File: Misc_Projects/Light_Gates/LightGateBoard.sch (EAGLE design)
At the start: 17 parts, among them T1 PHOTOTRANSISTOR

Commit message: Added changes to LightGateBoard
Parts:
- removed R3: 4.7k, 1-Passive Components:RES_AXIAL1/4W-0.3
- removed T1: PHOTOTRANSISTOR, 1-Active Components:PHOTOTRANSISTOR
- added JP5, JP6: (no value), GTOR - Connectors:PINHD-1X1
- added PH1: PHOTORESISTOR0N1, GTOR - Passive Components:PHOTORESISTOR0N1
- added R6: (no value), GTOR - Passive Components:POTENTIOMETER
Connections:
- net 3V3: now also PH1.1; no longer R3.2
- net GND: now also R6.A; no longer T1.E
- net SIG: now also JP5.1, JP6.1, PH1.2, R6.S; no longer R3.1, T1.C
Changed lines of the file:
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@@
 <layers>
 <layer number="1" name="Top" color="4" fill="1" visible="no" active="no"/>
+<layer number="2" name="Route2" color="16" fill="1" visible="no" active="no"/>
+<layer number="3" name="Route3" color="17" fill="1" visible="no" active="no"/>
+<layer number="4" name="Route4" color="18" fill="1" visible="no" active="no"/>
+<layer number="5" name="Route5" color="19" fill="1" visible="no" active="no"/>
+<layer number="6" name="Route6" color="25" fill="1" visible="no" active="no"/>
+<layer number="7" name="Route7" color="26" fill="1" visible="no" active="no"/>
+<layer number="8" name="Route8" color="27" fill="1" visible="no" active="no"/>
+<layer number="9" name="Route9" color="28" fill="1" visible="no" active="no"/>
+<layer number="10" name="Route10" color="29" fill="1" visible="no" active="no"/>
+<layer number="11" name="Route11" color="30" fill="1" visible="no" active="no"/>
+<layer number="12" name="Route12" color="20" fill="1" visible="no" active="no"/>
+<layer number="13" name="Route13" color="21" fill="1" visible="no" active="no"/>
+<layer number="14" name="Route14" color="22" fill="1" visible="no" active="no"/>
+<layer number="15" name="Route15" color="23" fill="1" visible="no" active="no"/>
 <layer number="16" name="Bottom" color="1" fill="1" visible="no" active="no"/>
 <layer number="17" name="Pads" color="2" fill="1" visible="no" active="no"/>
@@
 <part name="IC1" library="1-Active Components" deviceset="REG_5V_L7805" device="_HOR"/>
 <part name="U$3" library="1-Breakout Boards" deviceset="OLED_SSD1306" device=""/>
-<part name="T1" library="1-Active Components" deviceset="PHOTOTRANSISTOR" device=""/>
 <part name="LED1" library="1-Passive Components" deviceset="LED" device="-5MM" value="Green"/>
-<part name="R3" library="1-Passive Components" deviceset="RES_AXIAL" device="1/4W-0.3" package3d_urn="urn:adsk.eagle:package:23493/2" value="4.7k"/>
 <part name="V1" library="1-Active Components" deviceset="LOGIC_HEX_INVERTER_7404" device="N" package3d_urn="urn:adsk.eagle:package:16407/2"/>
 <part name="R4" library="1-Passive Components" deviceset="RES_AXIAL" device="1/4W-0.3" package3d_urn="urn:adsk.eagle:package:23493/2" value="220"/>
@@
 <part name="LED2" library="1-Passive Components" deviceset="LED" device="-5MM" value="Red"/>
 <part name="JP4" library="1-Connectors" deviceset="PINHD-1X3" device="" package3d_urn="urn:adsk.eagle:package:22458/2"/>
+<part name="PH1" library="GTOR - Passive Components" deviceset="PHOTORESISTOR" device="" package3d_urn="urn:adsk.eagle:package:22223/1" technology="0N1"/>
+<part name="R6" library="GTOR - Passive Components" deviceset="POTENTIOMETER" device="" package3d_urn="urn:adsk.eagle:package:22726/1"/>
+<part name="JP5" library="GTOR - Connectors" deviceset="PINHD-1X1" device="" package3d_urn="urn:adsk.eagle:package:22485/2"/>
+<part name="JP6" library="GTOR - Connectors" deviceset="PINHD-1X1" device="" package3d_urn="urn:adsk.eagle:package:22485/2"/>
 </parts>
 <sheets>
@@
 </instance>
 <instance part="U$3" gate="G$1" x="78.74" y="15.24" smashed="yes"/>
-<instance part="T1" gate="1" x="-104.14" y="58.42" smashed="yes">
-<attribute name="NAME" x="-99.06" y="60.96" size="1.778" layer="95"/>
-<attribute name="VALUE" x="-99.06" y="53.34" size="1.778" layer="96"/>
-</instance>
 <instance part="LED1" gate="LED" x="-38.1" y="88.9" smashed="yes" rot="R90">
 <attribute name="NAME" x="-33.528" y="92.456" size="1.778" layer="95" rot="R180"/>
 <attribute name="VALUE" x="-33.528" y="94.615" size="1.778" layer="96" rot="R180"/>
 </instance>
-<instance part="R3" gate="G$1" x="-101.6" y="76.2" smashed="yes" rot="R90">
-<attribute name="NAME" x="-103.0986" y="72.39" size="1.778" layer="95" rot="R90"/>
-<attribute name="VALUE" x="-98.298" y="72.39" size="1.778" layer="96" rot="R90"/>
-</instance>
 <instance part="V1" gate="/1" x="-73.66" y="88.9" smashed="yes">
 <attribute name="NAME" x="-78.74" y="94.615" size="2.032" layer="95"/>
@@
 <attribute name="NAME" x="62.23" y="56.515" size="1.778" layer="95"/>
 <attribute name="VALUE" x="62.23" y="43.18" size="1.778" layer="96"/>
+</instance>
+<instance part="PH1" gate="G$1" x="-93.98" y="38.1" smashed="yes">
+<attribute name="NAME" x="-91.44" y="38.1" size="1.778" layer="95"/>
+<attribute name="VALUE" x="-91.44" y="35.56" size="1.778" layer="96"/>
+</instance>
+<instance part="R6" gate="G$1" x="-99.06" y="25.4" smashed="yes">
+<attribute name="NAME" x="-102.489" y="21.59" size="1.778" layer="95" rot="R90"/>
+<attribute name="VALUE" x="-102.87" y="21.59" size="1.778" layer="96" rot="R90"/>
+</instance>
+<instance part="JP5" gate="G$1" x="-99.06" y="88.9" smashed="yes" rot="R180">
+<attribute name="NAME" x="-92.71" y="85.725" size="1.778" layer="95" rot="R180"/>
+<attribute name="VALUE" x="-92.71" y="93.98" size="1.778" layer="96" rot="R180"/>
+</instance>
+<instance part="JP6" gate="G$1" x="-99.06" y="81.28" smashed="yes" rot="R180">
+<attribute name="NAME" x="-92.71" y="78.105" size="1.778" layer="95" rot="R180"/>
+<attribute name="VALUE" x="-92.71" y="86.36" size="1.778" layer="96" rot="R180"/>
 </instance>
 </instances>
@@
 </segment>
 <segment>
-<pinref part="T1" gate="1" pin="E"/>
-<wire x1="-101.6" y1="53.34" x2="-101.6" y2="45.72" width="0.1524" layer="91"/>
-<label x="-106.68" y="48.26" size="1.778" layer="95"/>
-</segment>
-<segment>
 <pinref part="LED1" gate="LED" pin="C"/>
 <wire x1="-33.02" y1="88.9" x2="-25.4" y2="88.9" width="0.1524" layer="91"/>
@@
 <label x="55.88" y="50.8" size="1.778" layer="95"/>
 </segment>
+<segment>
+<wire x1="-99.06" y1="20.32" x2="-99.06" y2="12.7" width="0.1524" layer="91"/>
+<label x="-99.06" y="10.16" size="1.778" layer="95"/>
+<pinref part="R6" gate="G$1" pin="A"/>
+</segment>
 </net>
 <net name="5V" class="0">
@@
 </segment>
 <segment>
-<pinref part="R3" gate="G$1" pin="1"/>
-<pinref part="T1" gate="1" pin="C"/>
-<wire x1="-101.6" y1="71.12" x2="-101.6" y2="63.5" width="0.1524" layer="91"/>
-<label x="-106.68" y="68.58" size="1.778" layer="95"/>
-</segment>
-<segment>
 <pinref part="V1" gate="/1" pin="A"/>
+<label x="-88.9" y="88.9" size="1.778" layer="95"/>
 <wire x1="-83.82" y1="88.9" x2="-91.44" y2="88.9" width="0.1524" layer="91"/>
-<label x="-91.44" y="88.9" size="1.778" layer="95"/>
+<pinref part="JP5" gate="G$1" pin="1"/>
+<pinref part="JP6" gate="G$1" pin="1"/>
+<wire x1="-91.44" y1="88.9" x2="-96.52" y2="88.9" width="0.1524" layer="91"/>
+<wire x1="-96.52" y1="81.28" x2="-91.44" y2="81.28" width="0.1524" layer="91"/>
+<wire x1="-91.44" y1="81.28" x2="-91.44" y2="88.9" width="0.1524" layer="91"/>
+<junction x="-91.44" y="88.9"/>
 </segment>
 <segment>
@@
 <wire x1="2.54" y1="76.2" x2="-2.54" y2="76.2" width="0.1524" layer="91"/>
 <label x="-2.54" y="76.2" size="1.778" layer="95"/>
+</segment>
+<segment>
+<wire x1="-93.98" y1="33.02" x2="-93.98" y2="25.4" width="0.1524" layer="91"/>
+<label x="-99.06" y="30.48" size="1.778" layer="95"/>
+<pinref part="PH1" gate="G$1" pin="2"/>
+<pinref part="R6" gate="G$1" pin="S"/>
 </segment>
 </net>
@@
 </segment>
 <segment>
-<pinref part="R3" gate="G$1" pin="2"/>
-<wire x1="-101.6" y1="81.28" x2="-101.6" y2="88.9" width="0.1524" layer="91"/>
-<label x="-106.68" y="86.36" size="1.778" layer="95"/>
-</segment>
-<segment>
 <pinref part="R1" gate="G$1" pin="2"/>
 <wire x1="53.34" y1="33.02" x2="58.42" y2="33.02" width="0.1524" layer="91"/>
@@
 <label x="66.04" y="33.02" size="1.778" layer="95"/>
 </segment>
-</net>
+<segment>
+<pinref part="PH1" gate="G$1" pin="1"/>
+<label x="-93.98" y="60.96" size="1.778" layer="95"/>
+<wire x1="-93.98" y1="58.42" x2="-93.98" y2="43.18" width="0.1524" layer="91"/>
+</segment>
+</net>

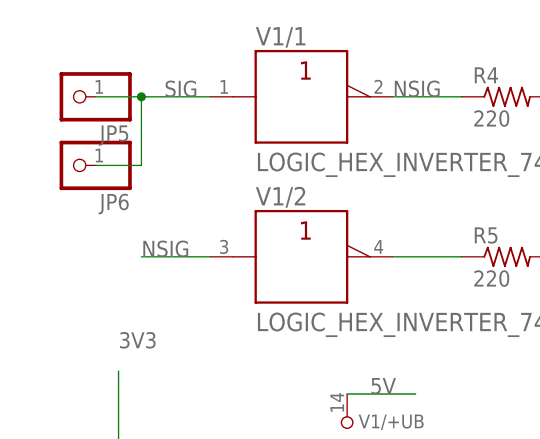
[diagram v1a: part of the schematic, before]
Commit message: Redid PCB with bigger traces and changed photodiode to photoresistor
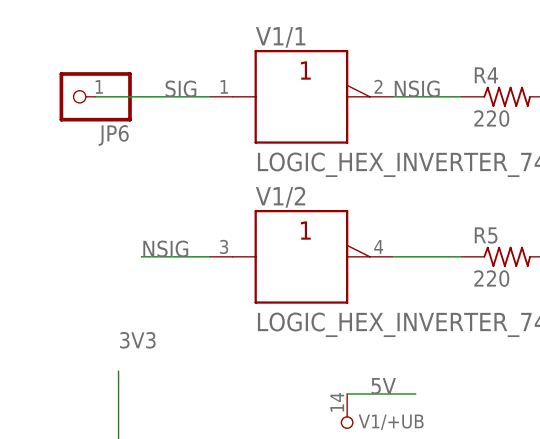
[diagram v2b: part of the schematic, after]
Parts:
- removed JP5: (no value), GTOR - Connectors:PINHD-1X1
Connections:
- net SIG: no longer JP5.1
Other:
- moved on the sheet: JP6
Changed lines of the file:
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@@
 <part name="PH1" library="GTOR - Passive Components" deviceset="PHOTORESISTOR" device="" package3d_urn="urn:adsk.eagle:package:22223/1" technology="0N1"/>
 <part name="R6" library="GTOR - Passive Components" deviceset="POTENTIOMETER" device="" package3d_urn="urn:adsk.eagle:package:22726/1"/>
-<part name="JP5" library="GTOR - Connectors" deviceset="PINHD-1X1" device="" package3d_urn="urn:adsk.eagle:package:22485/2"/>
 <part name="JP6" library="GTOR - Connectors" deviceset="PINHD-1X1" device="" package3d_urn="urn:adsk.eagle:package:22485/2"/>
 </parts>
@@
 <attribute name="VALUE" x="-102.87" y="21.59" size="1.778" layer="96" rot="R90"/>
 </instance>
-<instance part="JP5" gate="G$1" x="-99.06" y="88.9" smashed="yes" rot="R180">
+<instance part="JP6" gate="G$1" x="-99.06" y="88.9" smashed="yes" rot="R180">
 <attribute name="NAME" x="-92.71" y="85.725" size="1.778" layer="95" rot="R180"/>
 <attribute name="VALUE" x="-92.71" y="93.98" size="1.778" layer="96" rot="R180"/>
-</instance>
-<instance part="JP6" gate="G$1" x="-99.06" y="81.28" smashed="yes" rot="R180">
-<attribute name="NAME" x="-92.71" y="78.105" size="1.778" layer="95" rot="R180"/>
-<attribute name="VALUE" x="-92.71" y="86.36" size="1.778" layer="96" rot="R180"/>
 </instance>
 </instances>
@@
 <pinref part="V1" gate="/1" pin="A"/>
 <label x="-88.9" y="88.9" size="1.778" layer="95"/>
-<wire x1="-83.82" y1="88.9" x2="-91.44" y2="88.9" width="0.1524" layer="91"/>
-<pinref part="JP5" gate="G$1" pin="1"/>
+<wire x1="-83.82" y1="88.9" x2="-96.52" y2="88.9" width="0.1524" layer="91"/>
 <pinref part="JP6" gate="G$1" pin="1"/>
-<wire x1="-91.44" y1="88.9" x2="-96.52" y2="88.9" width="0.1524" layer="91"/>
-<wire x1="-96.52" y1="81.28" x2="-91.44" y2="81.28" width="0.1524" layer="91"/>
-<wire x1="-91.44" y1="81.28" x2="-91.44" y2="88.9" width="0.1524" layer="91"/>
-<junction x="-91.44" y="88.9"/>
-</segment>
-<segment>
+</segment>
+<segment>

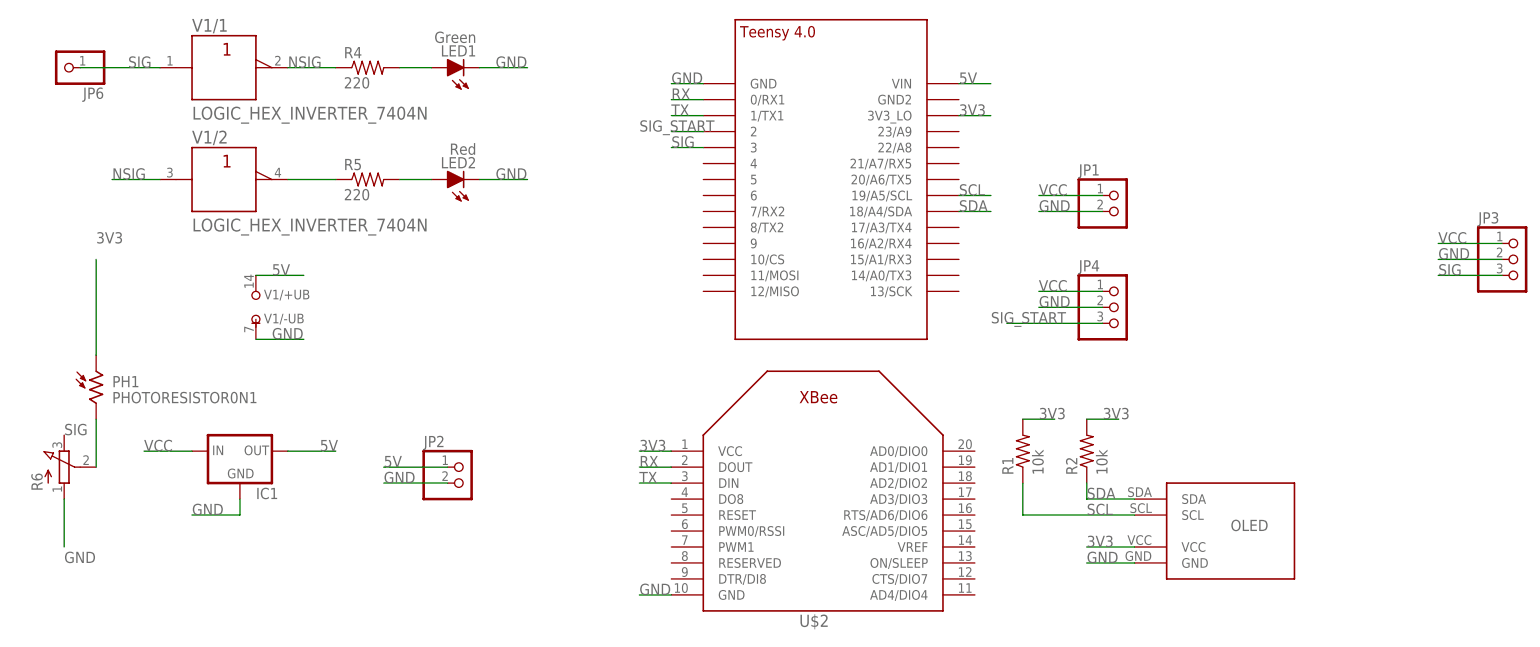
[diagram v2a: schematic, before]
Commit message: Fixed signal on PCB's, ready for manufacturing
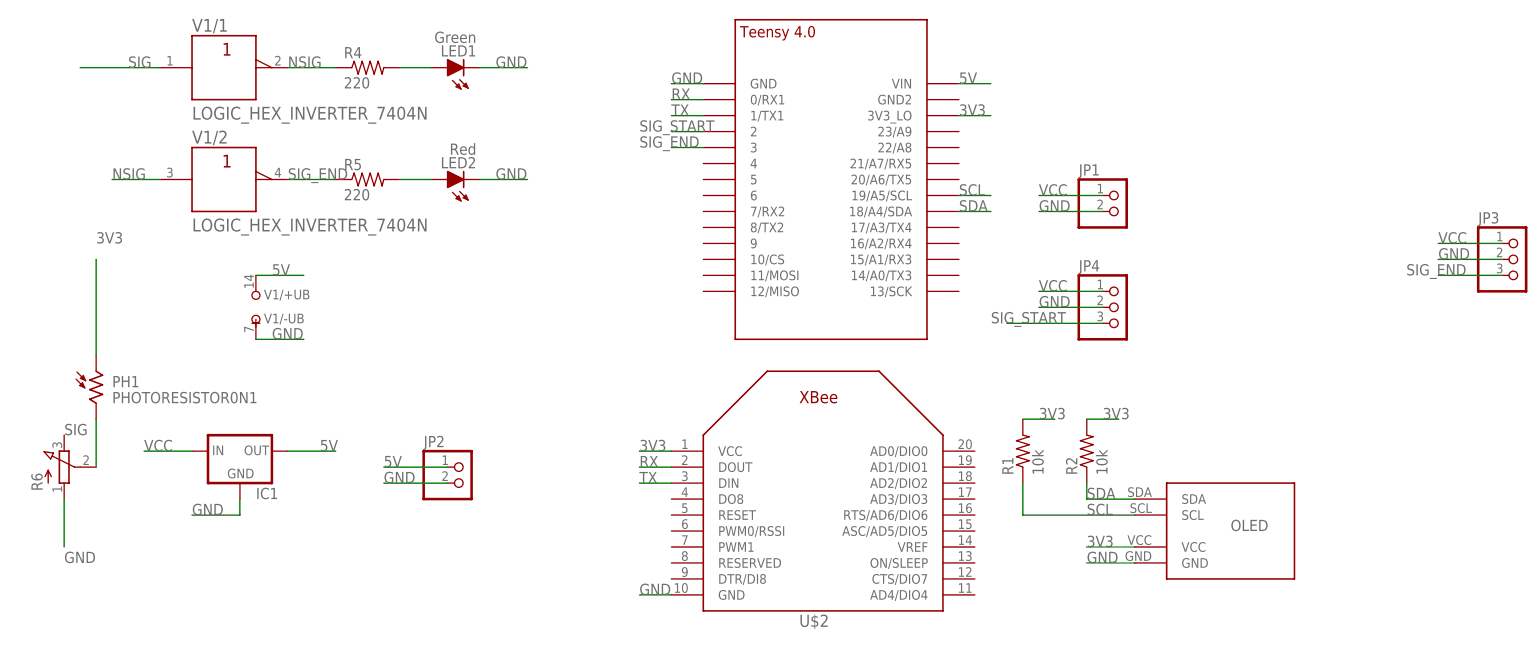
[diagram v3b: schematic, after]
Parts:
- removed JP6: (no value), GTOR - Connectors:PINHD-1X1
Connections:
- removed net N$6: R5.1, V1/2.Y
- new net SIG_END: JP3.3, R5.1, U$1.3, V1/2.Y
- net SIG: no longer JP3.3, JP6.1, U$1.3
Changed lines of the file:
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@@
 <part name="PH1" library="GTOR - Passive Components" deviceset="PHOTORESISTOR" device="" package3d_urn="urn:adsk.eagle:package:22223/1" technology="0N1"/>
 <part name="R6" library="GTOR - Passive Components" deviceset="POTENTIOMETER" device="" package3d_urn="urn:adsk.eagle:package:22726/1"/>
-<part name="JP6" library="GTOR - Connectors" deviceset="PINHD-1X1" device="" package3d_urn="urn:adsk.eagle:package:22485/2"/>
 </parts>
 <sheets>
@@
 <attribute name="VALUE" x="-102.87" y="21.59" size="1.778" layer="96" rot="R90"/>
 </instance>
-<instance part="JP6" gate="G$1" x="-99.06" y="88.9" smashed="yes" rot="R180">
-<attribute name="NAME" x="-92.71" y="85.725" size="1.778" layer="95" rot="R180"/>
-<attribute name="VALUE" x="-92.71" y="93.98" size="1.778" layer="96" rot="R180"/>
-</instance>
 </instances>
 <busses>
@@
 <net name="SIG" class="0">
 <segment>
-<wire x1="129.54" y1="55.88" x2="119.38" y2="55.88" width="0.1524" layer="91"/>
-<pinref part="JP3" gate="A" pin="3"/>
-<label x="119.38" y="55.88" size="1.778" layer="95"/>
-</segment>
-<segment>
 <pinref part="V1" gate="/1" pin="A"/>
 <label x="-88.9" y="88.9" size="1.778" layer="95"/>
 <wire x1="-83.82" y1="88.9" x2="-96.52" y2="88.9" width="0.1524" layer="91"/>
-<pinref part="JP6" gate="G$1" pin="1"/>
-</segment>
-<segment>
-<pinref part="U$1" gate="G$1" pin="3"/>
-<wire x1="2.54" y1="76.2" x2="-2.54" y2="76.2" width="0.1524" layer="91"/>
-<label x="-2.54" y="76.2" size="1.778" layer="95"/>
 </segment>
 <segment>
@@
 </segment>
 </net>
-<net name="N$6" class="0">
+<net name="SIG_END" class="0">
 <segment>
 <pinref part="V1" gate="/2" pin="Y"/>
 <pinref part="R5" gate="G$1" pin="1"/>
 <wire x1="-63.5" y1="71.12" x2="-55.88" y2="71.12" width="0.1524" layer="91"/>
-</segment>
-</net>
+<label x="-63.5" y="71.12" size="1.778" layer="95"/>
+</segment>
+<segment>
+<pinref part="U$1" gate="G$1" pin="3"/>
+<wire x1="2.54" y1="76.2" x2="-2.54" y2="76.2" width="0.1524" layer="91"/>
+<label x="-7.62" y="76.2" size="1.778" layer="95"/>
+</segment>
+<segment>
+<wire x1="129.54" y1="55.88" x2="119.38" y2="55.88" width="0.1524" layer="91"/>
+<pinref part="JP3" gate="A" pin="3"/>
+<label x="114.3" y="55.88" size="1.778" layer="95"/>
+</segment>
+</net>
